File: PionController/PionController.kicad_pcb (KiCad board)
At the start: 4 copper layers, 82 x 60 mm, 84 parts, among them J1 SM10B-ULHK-1TA1-ETB_HF_, J2 Conn_01x02, J3 Conn_01x02, J4 Conn_01x02, J6 Conn_01x02, J7 FTSH-107-01-L-DV-K-A, U1 STM32H743VITx, U2 TLV75733PDBV, U3 ISO1050DUB, U4 ISO1050DUB, U5 CA-IS3740HN, X1 ASE-16.00MHz, Y2 32.768kHZ

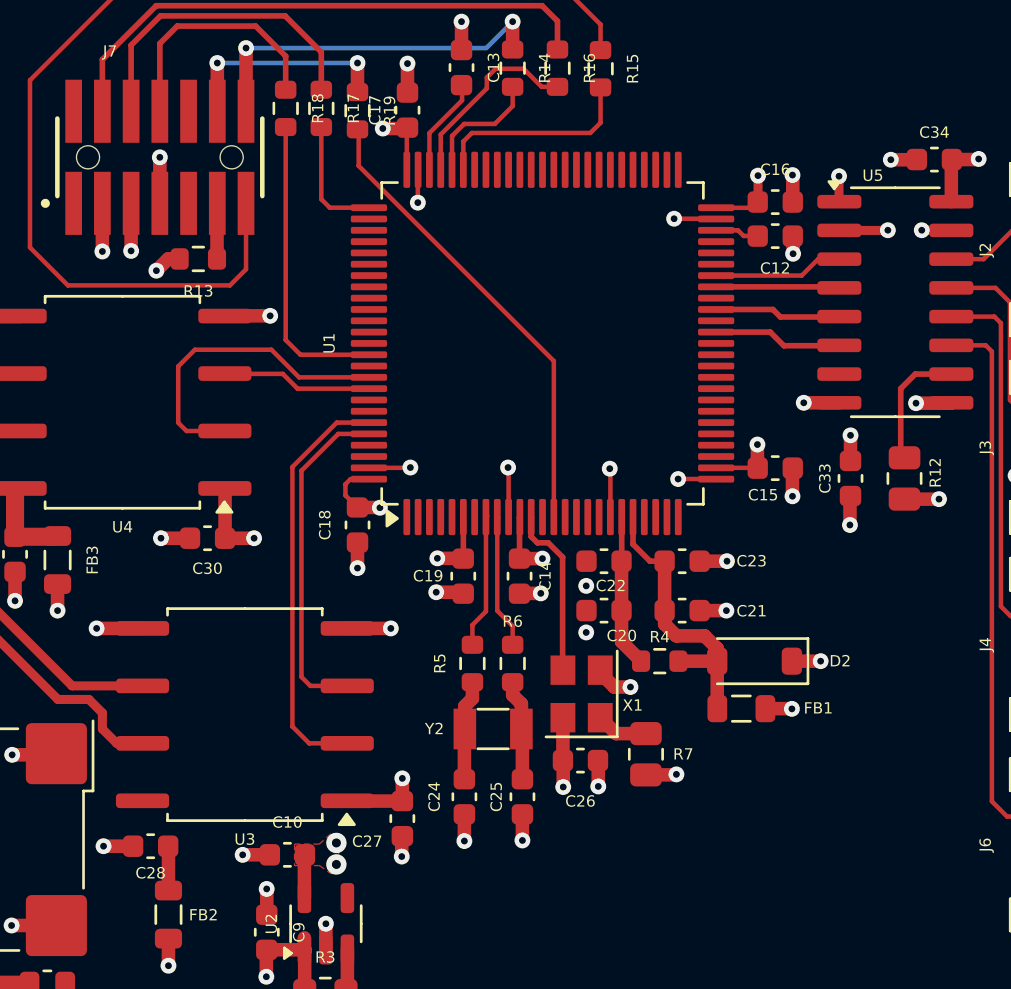
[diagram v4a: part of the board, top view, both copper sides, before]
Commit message: Fixing one forgotten decoupling capacitor.
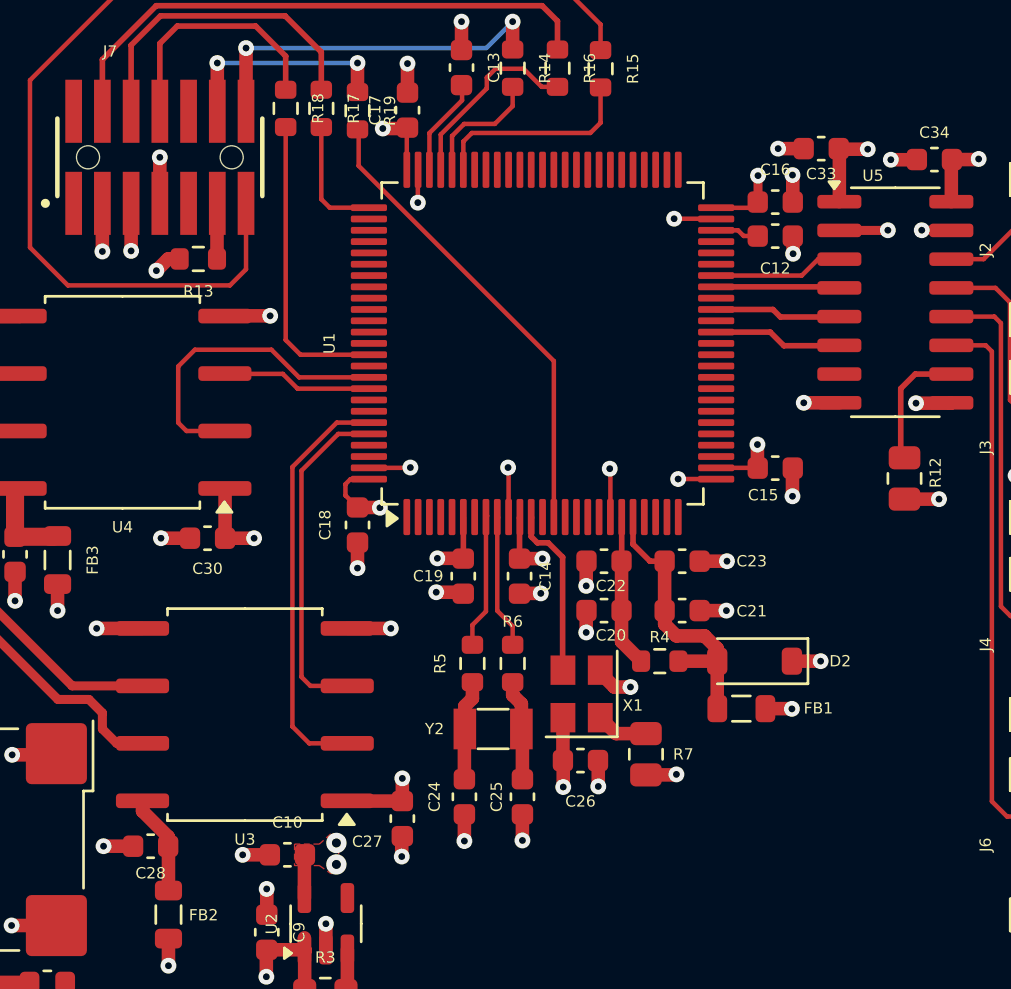
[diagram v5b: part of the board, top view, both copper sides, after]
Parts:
- moved C33 14.6 mm to (161.8, 79.1), turned to 180 degrees
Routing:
- net Net-(U3-VCC2): track 1.99 -> 4.44 mm
- net GND: track 101.6 -> 103.6 mm
- net +3.3V: track 38.7 -> 39.9 mm, vias 17 -> 16
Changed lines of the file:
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@@
 	(footprint "Capacitor_SMD:C_0603_1608Metric"
 		(layer "F.Cu")
-		(at 163.0934 93.6498 90)
+		(at 161.798 79.0702 180)
 		(descr "Capacitor SMD 0603 (1608 Metric), square (rectangular) end terminal, IPC_7351 nominal, (Body size source: IPC-SM-782 page 76, https://www.pcb-3d.com/wordpress/wp-content/uploads/ipc-sm-782a_amendment_1_and_2.pdf), generated with kicad-footprint-generator")
 		(tags "capacitor")
 		(property "Reference" "C33"
-			(at 0 -1.1176 90)
+			(at 0 -1.1176 360)
 			(layer "F.SilkS")
 			(effects
@@
 		)
 		(property "Value" "100nF"
-			(at 0 1.43 90)
+			(at 0 1.43 360)
 			(layer "F.Fab")
 			(effects
@@
 		)
 		(property "Footprint" "Capacitor_SMD:C_0603_1608Metric"
-			(at 0 0 90)
+			(at 0 0 180)
 			(unlocked yes)
 			(layer "F.Fab")
@@
 		)
 		(property "Datasheet" ""
-			(at 0 0 90)
+			(at 0 0 180)
 			(unlocked yes)
 			(layer "F.Fab")
@@
 		)
 		(property "Description" "Unpolarized capacitor, small symbol"
-			(at 0 0 90)
+			(at 0 0 180)
 			(unlocked yes)
 			(layer "F.Fab")
@@
 		)
 		(property "LCSC" "C91183"
-			(at 0 0 90)
+			(at 0 0 180)
 			(unlocked yes)
 			(layer "F.Fab")
@@
 		)
 		(property "Manufacturer" "CC0603JRX7R9BB104"
-			(at 0 0 90)
+			(at 0 0 180)
 			(unlocked yes)
 			(layer "F.Fab")
@@
 		)
 		(property "Comment" ""
-			(at 0 0 90)
+			(at 0 0 180)
 			(unlocked yes)
 			(layer "F.Fab")
@@
 		(attr smd)
 		(fp_line
-			(start -0.14058 -0.51)
-			(end 0.14058 -0.51)
+			(start -0.14058 0.51)
+			(end 0.14058 0.51)
 			(stroke
 				(width 0.12)
@@
 		)
 		(fp_line
-			(start -0.14058 0.51)
-			(end 0.14058 0.51)
+			(start -0.14058 -0.51)
+			(end 0.14058 -0.51)
 			(stroke
 				(width 0.12)
@@
 		)
 		(fp_line
-			(start 1.48 -0.73)
-			(end 1.48 0.73)
+			(start 1.48 0.73)
+			(end -1.48 0.73)
 			(stroke
 				(width 0.05)
@@
 		)
 		(fp_line
-			(start -1.48 -0.73)
-			(end 1.48 -0.73)
+			(start 1.48 -0.73)
+			(end 1.48 0.73)
 			(stroke
 				(width 0.05)
@@
 		)
 		(fp_line
-			(start 1.48 0.73)
-			(end -1.48 0.73)
+			(start -1.48 0.73)
+			(end -1.48 -0.73)
 			(stroke
 				(width 0.05)
@@
 		)
 		(fp_line
-			(start -1.48 0.73)
-			(end -1.48 -0.73)
+			(start -1.48 -0.73)
+			(end 1.48 -0.73)
 			(stroke
 				(width 0.05)
@@
 		)
 		(fp_line
-			(start 0.8 -0.4)
-			(end 0.8 0.4)
+			(start 0.8 0.4)
+			(end -0.8 0.4)
 			(stroke
 				(width 0.1)
@@
 		)
 		(fp_line
-			(start -0.8 -0.4)
-			(end 0.8 -0.4)
+			(start 0.8 -0.4)
+			(end 0.8 0.4)
 			(stroke
 				(width 0.1)
@@
 		)
 		(fp_line
-			(start 0.8 0.4)
-			(end -0.8 0.4)
+			(start -0.8 0.4)
+			(end -0.8 -0.4)
 			(stroke
 				(width 0.1)
@@
 		)
 		(fp_line
-			(start -0.8 0.4)
-			(end -0.8 -0.4)
+			(start -0.8 -0.4)
+			(end 0.8 -0.4)
 			(stroke
 				(width 0.1)
@@
 		)
 		(fp_text user "${REFERENCE}"
-			(at 0 0 90)
+			(at 0 0 360)
 			(layer "F.Fab")
 			(effects
@@
 		)
 		(pad "1" smd roundrect
-			(at -0.775 0 90)
+			(at -0.775 0 180)
 			(size 0.9 0.95)
 			(layers "F.Cu" "F.Paste" "F.Mask")
@@
 		)
 		(pad "2" smd roundrect
-			(at 0.775 0 90)
+			(at 0.775 0 180)
 			(size 0.9 0.95)
 			(layers "F.Cu" "F.Paste" "F.Mask")
@@
 		(tags "capacitor")
 		(property "Reference" "C20"
-			(at 0.7874 1.1176 360)
+			(at 0.3048 1.0922 360)
 			(layer "F.SilkS")
 			(effects
@@
 	)
 	(segment
-		(start 163.0934 92.8748)
-		(end 163.0934 91.7448)
+		(start 161.023 79.0702)
+		(end 159.893 79.0702)
 		(width 0.6)
 		(layer "F.Cu")
@@
 	)
 	(segment
+		(start 151.4094 97.3198)
+		(end 151.4218 97.3074)
+		(width 0.6)
+		(layer "F.Cu")
+		(net 68)
+	)
+	(segment
 		(start 143.51 76.5934)
 		(end 143.51 75.311)
@@
 	)
 	(segment
+		(start 151.4094 99.5042)
+		(end 151.4218 99.4918)
+		(width 0.6)
+		(layer "F.Cu")
+		(net 68)
+	)
+	(segment
 		(start 111.9112 89.9142)
 		(end 113.2858 89.9142)
@@
 	)
 	(segment
+		(start 151.4094 100.457)
+		(end 151.4094 99.5042)
+		(width 0.6)
+		(layer "F.Cu")
+		(net 68)
+	)
+	(segment
 		(start 147.979 93.1912)
 		(end 147.979 95.3558)
@@
 	)
 	(segment
+		(start 151.4094 98.3996)
+		(end 151.4094 97.3198)
+		(width 0.6)
+		(layer "F.Cu")
+		(net 68)
+	)
+	(segment
 		(start 160.5534 82.949)
 		(end 160.541 82.9366)
@@
 	)
 	(via
-		(at 163.0934 91.7448)
+		(at 159.893 79.0702)
 		(size 0.7)
 		(drill 0.3)
@@
 	)
 	(segment
-		(start 162.5854 80.2894)
-		(end 162.5854 81.4016)
-		(width 0.4)
-		(layer "F.Cu")
-		(net 76)
-	)
-	(segment
-		(start 163.068 95.7072)
-		(end 163.068 94.4502)
+		(start 163.8554 79.0956)
+		(end 162.5984 79.0956)
 		(width 0.6)
 		(layer "F.Cu")
@@
 	)
 	(segment
+		(start 162.5996 79.0968)
+		(end 162.5984 79.0956)
+		(width 0.6)
+		(layer "F.Cu")
+		(net 76)
+	)
+	(segment
 		(start 135.4458 96.2914)
 		(end 135.4458 94.1016)
@@
 	)
 	(segment
+		(start 162.5996 81.4158)
+		(end 162.5996 79.0968)
+		(width 0.6)
+		(layer "F.Cu")
+		(net 76)
+	)
+	(segment
 		(start 144.8308 97.1804)
 		(end 145.9614 97.1804)
@@
 	)
 	(segment
-		(start 163.068 94.4502)
-		(end 163.0934 94.4248)
+		(start 162.5984 79.0956)
+		(end 162.573 79.0702)
 		(width 0.4)
 		(layer "F.Cu")
@@
 	)
 	(via
-		(at 162.5854 80.2894)
-		(size 0.7)
-		(drill 0.3)
-		(layers "F.Cu" "B.Cu")
-		(free yes)
-		(net 76)
-	)
-	(via
 		(at 142.4178 78.1812)
 		(size 0.7)
@@
 	)
 	(via
-		(at 163.068 95.7072)
+		(at 163.8554 79.0956)
 		(size 0.7)
 		(drill 0.3)
@@
 	)
 	(segment
-		(start 132.9436 109.9182)
-		(end 132.9312 109.9058)
+		(start 132.9312 109.4889)
+		(end 131.7968 108.3545)
 		(width 0.6)
 		(layer "F.Cu")
@@
 	)
 	(segment
-		(start 131.813 107.9154)
+		(start 131.7968 108.3545)
 		(end 131.7968 107.8992)
 		(width 0.6)
 		(layer "F.Cu")
+		(net 81)
+	)
+	(segment
+		(start 132.9312 109.9058)
+		(end 132.9312 109.4889)
+		(width 0.6)
+		(layer "F.Cu")
+		(net 81)
+	)
+	(segment
+		(start 132.9436 109.9182)
+		(end 132.9312 109.9058)
+		(width 0.6)
+		(layer "F.Cu")
